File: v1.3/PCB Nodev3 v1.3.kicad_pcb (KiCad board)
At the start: 2 copper layers, 120 x 50 mm, 56 parts, among them P1 ESP32 NODEMCU DEVKIT1 LEFT HE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, P2 ESP32 NODEMCU DEVKIT1 RIGHT H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, Q1 Q_NPN_BEC, Q2 Q_NPN_BEC, U1 MFRC522, U2 3,0, U3 3,0, U4 3,0, U5 3,0, U6 Tooling Hole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

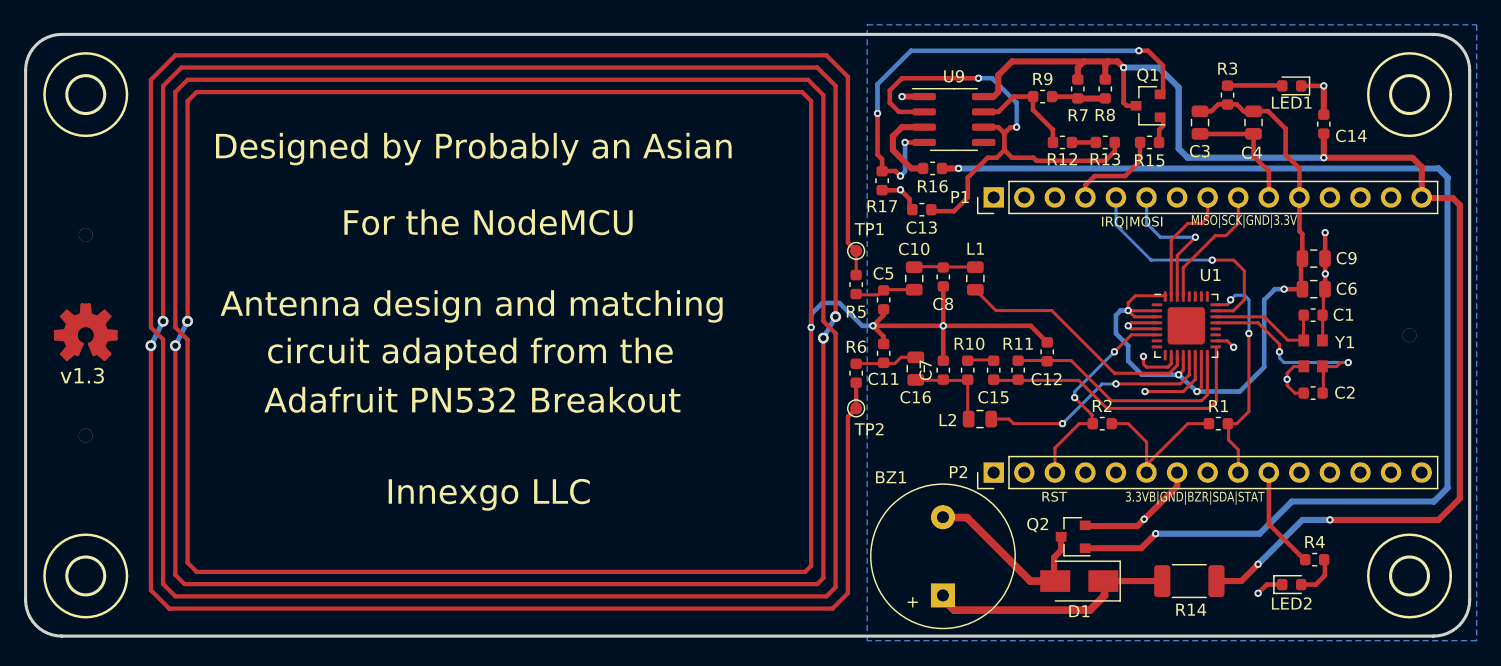
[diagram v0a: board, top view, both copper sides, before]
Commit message: Ran DRC, buzzer may lean over the edge.
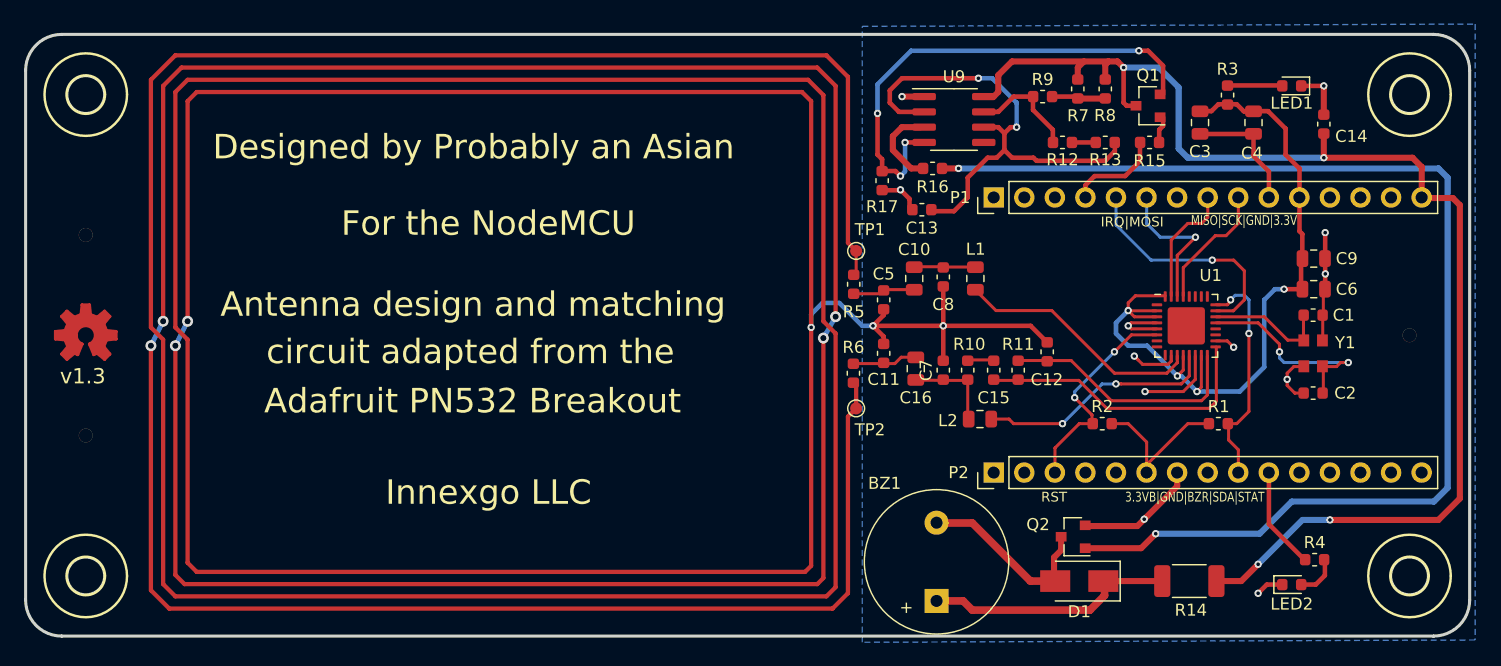
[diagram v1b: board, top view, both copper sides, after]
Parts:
- moved BZ1 0.70 mm to (111.6, 101.5)
- moved R6 0.23 mm to (104.7, 85.9)
- moved R5 0.20 mm to (104.7, 78.5)
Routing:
- net +3V3: track 63.4 -> 62.4 mm
